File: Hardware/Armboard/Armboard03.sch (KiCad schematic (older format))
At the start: 8 parts

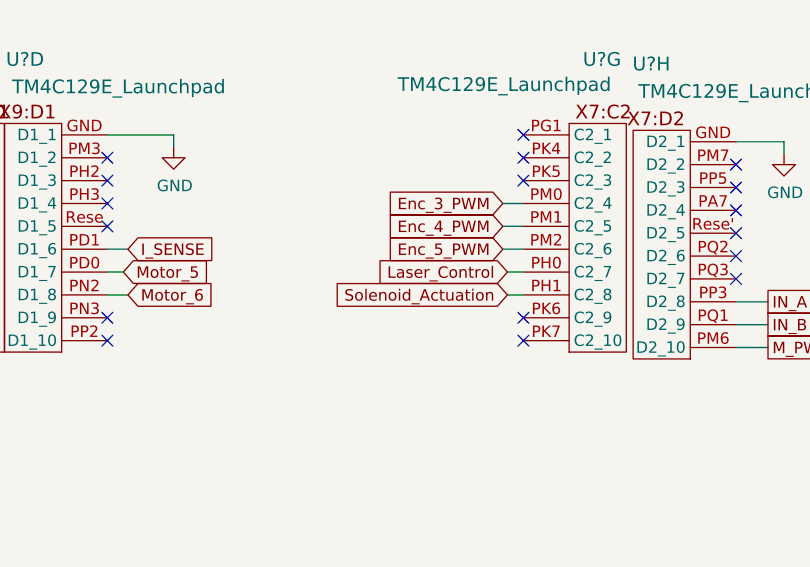
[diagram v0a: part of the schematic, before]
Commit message: Deleted laser and solenoid
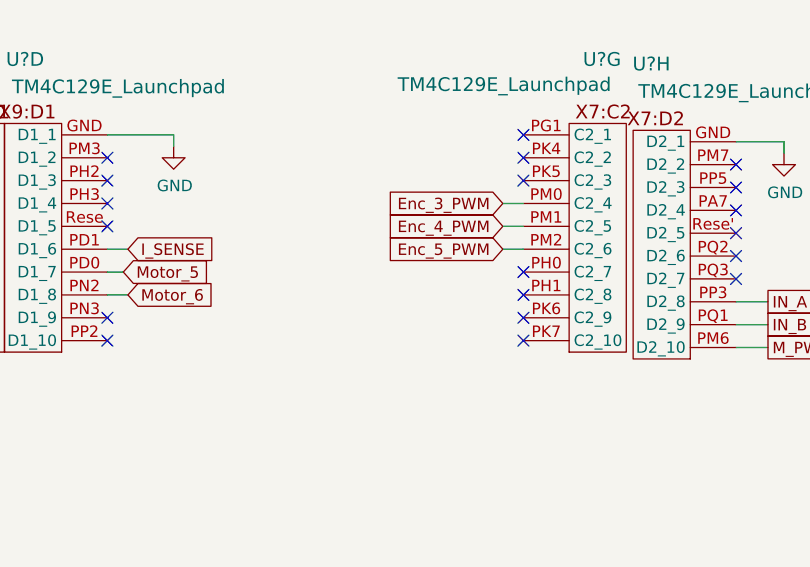
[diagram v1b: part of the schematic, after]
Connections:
- net Laser_Control: no longer names the net of U?.PH0 (C2_7)
- net Solenoid_Actuation: no longer names the net of U?.PH1 (C2_8)
- no-connect marks 43 -> 45
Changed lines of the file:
@@
 $Descr A 11000 8500
 encoding utf-8
-Sheet 3 9
+Sheet 3 7
 Title ""
 Date ""
@@
 Wire Wire Line
 	3610 3350 3540 3350
-Text GLabel 6250 5170 0    50   Input ~ 0
-Laser_Control
-Wire Wire Line
-	6320 5170 6250 5170
-Text GLabel 6250 5270 0    50   Input ~ 0
-Solenoid_Actuation
-Wire Wire Line
-	6320 5270 6250 5270
 Text GLabel 3540 2650 0    50   Input ~ 0
 Rx_1_Tiva
@@
 Wire Wire Line
 	6120 3340 6200 3340
+NoConn ~ 6320 5170
+NoConn ~ 6320 5270
 $EndSCHEMATC

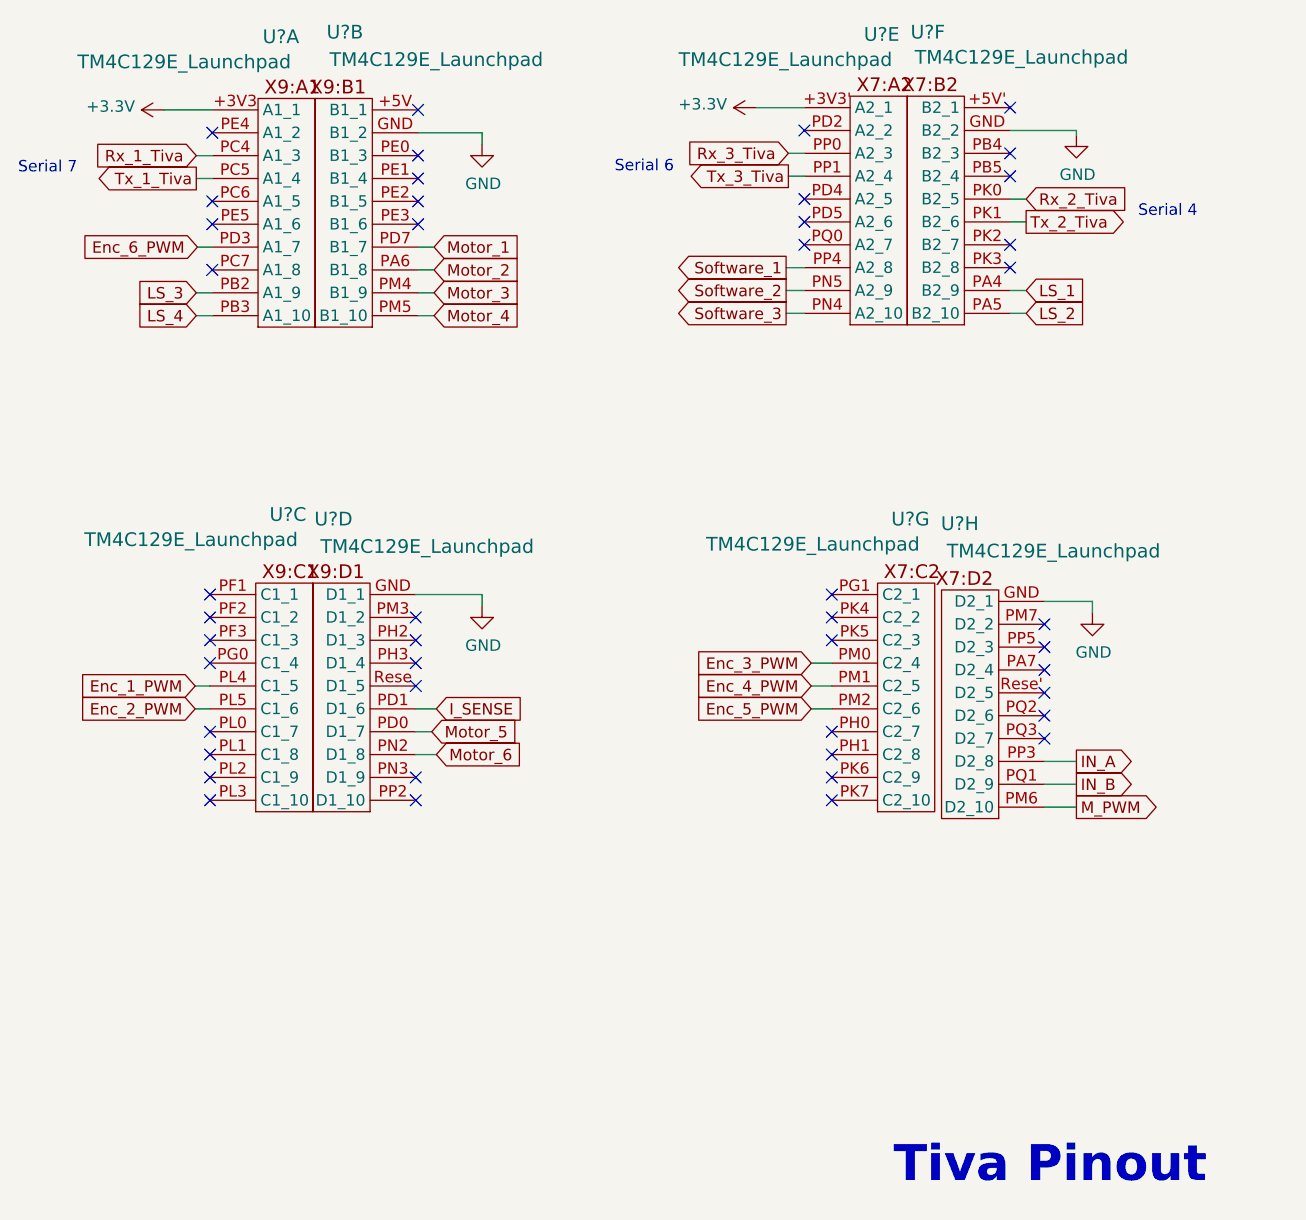
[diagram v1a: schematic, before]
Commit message: Assigned R/L/C footprints
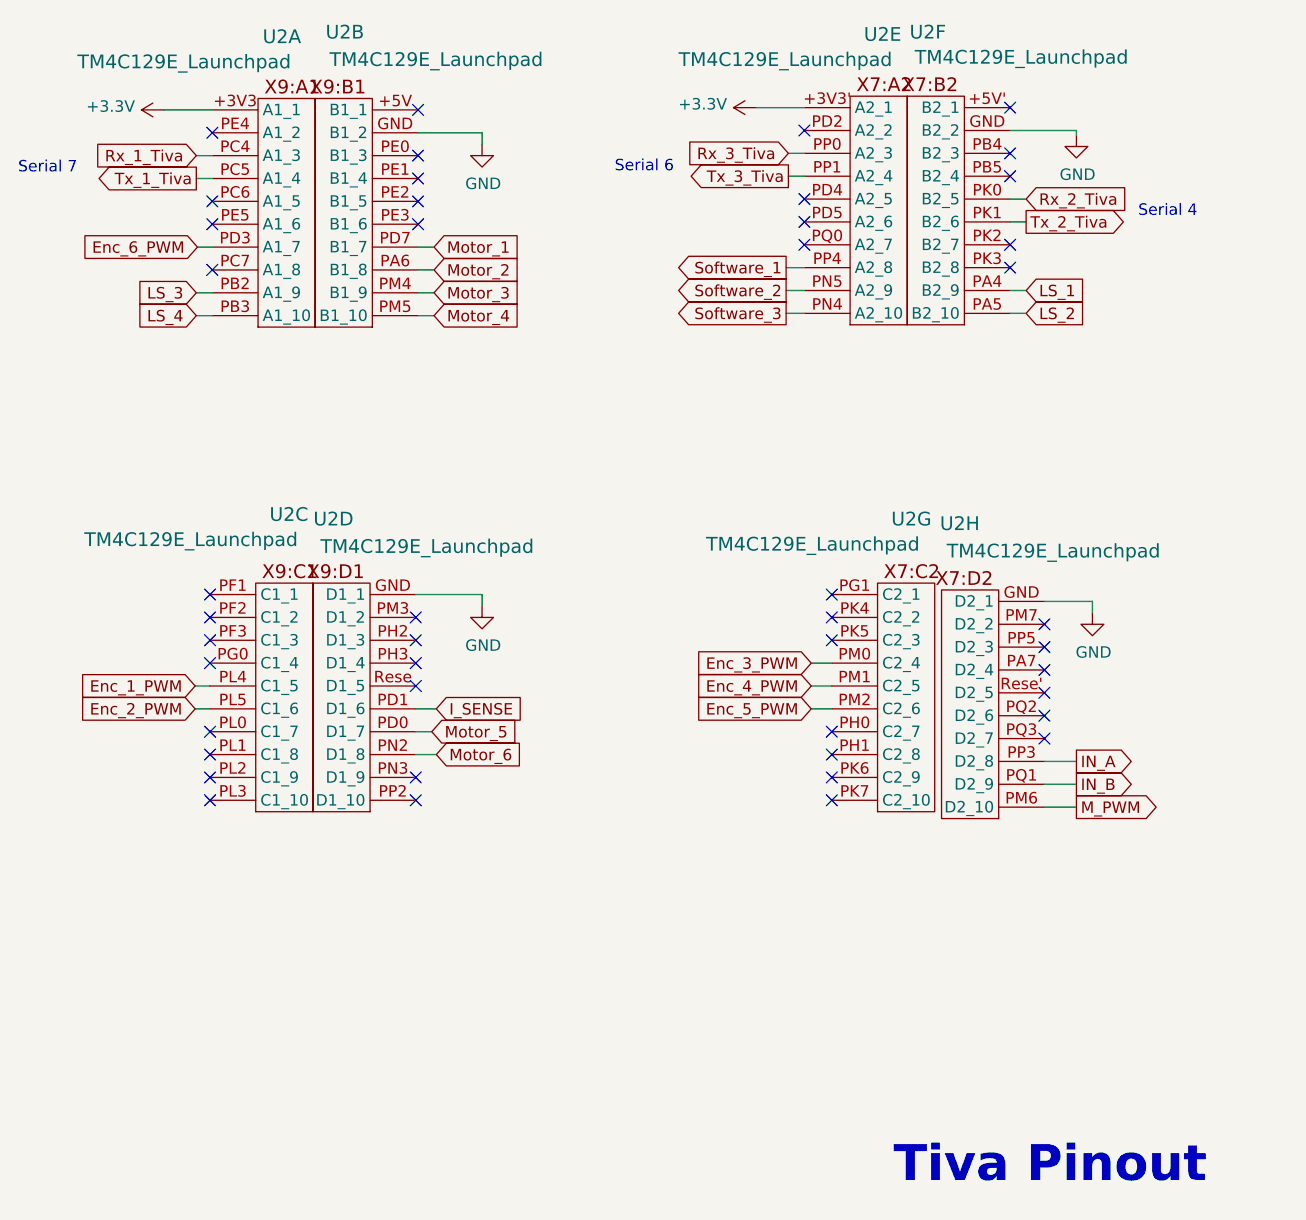
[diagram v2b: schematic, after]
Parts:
- gave numbers to parts that had none: 1
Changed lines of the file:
@@
 $EndDescr
 $Comp
-L Armboard-rescue:TM4C129E_Launchpad-MRDT_Shields-Armboard-rescue U?
+L Armboard-rescue:TM4C129E_Launchpad-MRDT_Shields-Armboard-rescue U2
 U 1 1 5F752485
 P 3810 3400
-F 0 "U?" H 3830 4670 60  0000 L CNN
+F 0 "U2" H 3830 4670 60  0000 L CNN
 F 1 "TM4C129E_Launchpad" H 3020 4560 60  0000 L CNN
 F 2 "" H 3810 3400 60  0001 C CNN
@@
 $EndComp
 $Comp
-L Armboard-rescue:TM4C129E_Launchpad-MRDT_Shields-Armboard-rescue U?
+L Armboard-rescue:TM4C129E_Launchpad-MRDT_Shields-Armboard-rescue U2
 U 2 1 5F752EEB
 P 4310 3400
-F 0 "U?" H 4430 4690 60  0000 C CNN
+F 0 "U2" H 4430 4690 60  0000 C CNN
 F 1 "TM4C129E_Launchpad" H 4030 4570 60  0000 C CNN
 F 2 "" H 4310 3400 60  0001 C CNN
@@
 $EndComp
 $Comp
-L Armboard-rescue:TM4C129E_Launchpad-MRDT_Shields-Armboard-rescue U?
+L Armboard-rescue:TM4C129E_Launchpad-MRDT_Shields-Armboard-rescue U2
 U 3 1 5F753E3C
 P 3800 5520
-F 0 "U?" H 3860 6820 60  0000 L CNN
+F 0 "U2" H 3860 6820 60  0000 L CNN
 F 1 "TM4C129E_Launchpad" H 3050 6710 60  0000 L CNN
 F 2 "" H 3800 5520 60  0001 C CNN
@@
 $EndComp
 $Comp
-L Armboard-rescue:TM4C129E_Launchpad-MRDT_Shields-Armboard-rescue U?
+L Armboard-rescue:TM4C129E_Launchpad-MRDT_Shields-Armboard-rescue U2
 U 5 1 5F755C93
 P 6400 3390
-F 0 "U?" H 6460 4660 60  0000 L CNN
+F 0 "U2" H 6460 4660 60  0000 L CNN
 F 1 "TM4C129E_Launchpad" H 5650 4550 60  0000 L CNN
 F 2 "" H 6400 3390 60  0001 C CNN
@@
 $EndComp
 $Comp
-L Armboard-rescue:TM4C129E_Launchpad-MRDT_Shields-Armboard-rescue U?
+L Armboard-rescue:TM4C129E_Launchpad-MRDT_Shields-Armboard-rescue U2
 U 6 1 5F7570A2
 P 6900 3390
-F 0 "U?" H 7060 4670 60  0000 C CNN
+F 0 "U2" H 7060 4670 60  0000 C CNN
 F 1 "TM4C129E_Launchpad" H 6650 4560 60  0000 C CNN
 F 2 "" H 6900 3390 60  0001 C CNN
@@
 $EndComp
 $Comp
-L Armboard-rescue:TM4C129E_Launchpad-MRDT_Shields-Armboard-rescue U?
+L Armboard-rescue:TM4C129E_Launchpad-MRDT_Shields-Armboard-rescue U2
 U 7 1 5F757FE4
 P 6520 5520
-F 0 "U?" H 6580 6800 60  0000 L CNN
+F 0 "U2" H 6580 6800 60  0000 L CNN
 F 1 "TM4C129E_Launchpad" H 5770 6690 60  0000 L CNN
 F 2 "" H 6520 5520 60  0001 C CNN
@@
 $EndComp
 $Comp
-L Armboard-rescue:TM4C129E_Launchpad-MRDT_Shields-Armboard-rescue U?
+L Armboard-rescue:TM4C129E_Launchpad-MRDT_Shields-Armboard-rescue U2
 U 8 1 5F7598C0
 P 7050 5550
-F 0 "U?" H 7220 6840 60  0000 C CNN
+F 0 "U2" H 7220 6840 60  0000 C CNN
 F 1 "TM4C129E_Launchpad" H 6810 6720 60  0000 C CNN
 F 2 "" H 7050 5550 60  0001 C CNN
@@
 $EndComp
 $Comp
-L power:GND #PWR?
+L power:GND #PWR015
 U 1 1 5F83BEC8
 P 4790 2600
-F 0 "#PWR?" H 4790 2350 50  0001 C CNN
+F 0 "#PWR015" H 4790 2350 50  0001 C CNN
 F 1 "GND" H 4795 2427 50  0000 C CNN
 F 2 "" H 4790 2600 50  0001 C CNN
@@
 	4790 2550 4790 2600
 $Comp
-L power:+3.3V #PWR?
+L power:+3.3V #PWR014
 U 1 1 5F83D247
 P 3400 2450
-F 0 "#PWR?" H 3400 2300 50  0001 C CNN
+F 0 "#PWR014" H 3400 2300 50  0001 C CNN
 F 1 "+3.3V" V 3415 2578 50  0000 L CNN
 F 2 "" H 3400 2450 50  0001 C CNN
@@
 	3400 2450 3610 2450
 $Comp
-L power:+3.3V #PWR?
+L power:+3.3V #PWR017
 U 1 1 5F83FA68
 P 5990 2440
-F 0 "#PWR?" H 5990 2290 50  0001 C CNN
+F 0 "#PWR017" H 5990 2290 50  0001 C CNN
 F 1 "+3.3V" V 6005 2568 50  0000 L CNN
 F 2 "" H 5990 2440 50  0001 C CNN
@@
 	5990 2440 6200 2440
 $Comp
-L power:GND #PWR?
+L power:GND #PWR018
 U 1 1 5F83FD93
 P 7390 2560
-F 0 "#PWR?" H 7390 2310 50  0001 C CNN
+F 0 "#PWR018" H 7390 2310 50  0001 C CNN
 F 1 "GND" H 7395 2387 50  0000 C CNN
 F 2 "" H 7390 2560 50  0001 C CNN
@@
 $EndComp
 $Comp
-L power:GND #PWR?
+L power:GND #PWR016
 U 1 1 5F83FFBB
 P 4790 4620
-F 0 "#PWR?" H 4790 4370 50  0001 C CNN
+F 0 "#PWR016" H 4790 4370 50  0001 C CNN
 F 1 "GND" H 4795 4447 50  0000 C CNN
 F 2 "" H 4790 4620 50  0001 C CNN
@@
 	4790 4570 4790 4620
 $Comp
-L power:GND #PWR?
+L power:GND #PWR019
 U 1 1 5F8401EF
 P 7460 4650
-F 0 "#PWR?" H 7460 4400 50  0001 C CNN
+F 0 "#PWR019" H 7460 4400 50  0001 C CNN
 F 1 "GND" H 7465 4477 50  0000 C CNN
 F 2 "" H 7460 4650 50  0001 C CNN
@@
 	4500 4570 4790 4570
 $Comp
-L Armboard-rescue:TM4C129E_Launchpad-MRDT_Shields-Armboard-rescue U?
+L Armboard-rescue:TM4C129E_Launchpad-MRDT_Shields-Armboard-rescue U2
 U 4 1 5F754D60
 P 4300 5520
-F 0 "U?" H 4460 6800 60  0000 C CNN
+F 0 "U2" H 4460 6800 60  0000 C CNN
 F 1 "TM4C129E_Launchpad" H 4050 6680 60  0000 C CNN
 F 2 "" H 4300 5520 60  0001 C CNN

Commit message: Imported footprints to layout
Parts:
- U2: footprint (none) -> MRDT_Shields:TM4C129E_Launchpad_FULL_SMD_BOTTOM
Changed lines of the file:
@@
 F 0 "U2" H 3830 4670 60  0000 L CNN
 F 1 "TM4C129E_Launchpad" H 3020 4560 60  0000 L CNN
-F 2 "" H 3810 3400 60  0001 C CNN
+F 2 "MRDT_Shields:TM4C129E_Launchpad_FULL_SMD_BOTTOM" H 3810 3400 60  0001 C CNN
 F 3 "" H 3810 3400 60  0001 C CNN
 	1    3810 3400
@@
 F 0 "U2" H 4430 4690 60  0000 C CNN
 F 1 "TM4C129E_Launchpad" H 4030 4570 60  0000 C CNN
-F 2 "" H 4310 3400 60  0001 C CNN
+F 2 "MRDT_Shields:TM4C129E_Launchpad_FULL_SMD_BOTTOM" H 4310 3400 60  0001 C CNN
 F 3 "" H 4310 3400 60  0001 C CNN
 	2    4310 3400
@@
 F 0 "U2" H 3860 6820 60  0000 L CNN
 F 1 "TM4C129E_Launchpad" H 3050 6710 60  0000 L CNN
-F 2 "" H 3800 5520 60  0001 C CNN
+F 2 "MRDT_Shields:TM4C129E_Launchpad_FULL_SMD_BOTTOM" H 3800 5520 60  0001 C CNN
 F 3 "" H 3800 5520 60  0001 C CNN
 	3    3800 5520
@@
 F 0 "U2" H 6460 4660 60  0000 L CNN
 F 1 "TM4C129E_Launchpad" H 5650 4550 60  0000 L CNN
-F 2 "" H 6400 3390 60  0001 C CNN
+F 2 "MRDT_Shields:TM4C129E_Launchpad_FULL_SMD_BOTTOM" H 6400 3390 60  0001 C CNN
 F 3 "" H 6400 3390 60  0001 C CNN
 	5    6400 3390
@@
 F 0 "U2" H 7060 4670 60  0000 C CNN
 F 1 "TM4C129E_Launchpad" H 6650 4560 60  0000 C CNN
-F 2 "" H 6900 3390 60  0001 C CNN
+F 2 "MRDT_Shields:TM4C129E_Launchpad_FULL_SMD_BOTTOM" H 6900 3390 60  0001 C CNN
 F 3 "" H 6900 3390 60  0001 C CNN
 	6    6900 3390
@@
 F 0 "U2" H 6580 6800 60  0000 L CNN
 F 1 "TM4C129E_Launchpad" H 5770 6690 60  0000 L CNN
-F 2 "" H 6520 5520 60  0001 C CNN
+F 2 "MRDT_Shields:TM4C129E_Launchpad_FULL_SMD_BOTTOM" H 6520 5520 60  0001 C CNN
 F 3 "" H 6520 5520 60  0001 C CNN
 	7    6520 5520
@@
 F 0 "U2" H 7220 6840 60  0000 C CNN
 F 1 "TM4C129E_Launchpad" H 6810 6720 60  0000 C CNN
-F 2 "" H 7050 5550 60  0001 C CNN
+F 2 "MRDT_Shields:TM4C129E_Launchpad_FULL_SMD_BOTTOM" H 7050 5550 60  0001 C CNN
 F 3 "" H 7050 5550 60  0001 C CNN
 	8    7050 5550
@@
 F 0 "U2" H 4460 6800 60  0000 C CNN
 F 1 "TM4C129E_Launchpad" H 4050 6680 60  0000 C CNN
-F 2 "" H 4300 5520 60  0001 C CNN
+F 2 "MRDT_Shields:TM4C129E_Launchpad_FULL_SMD_BOTTOM" H 4300 5520 60  0001 C CNN
 F 3 "" H 4300 5520 60  0001 C CNN
 	4    4300 5520

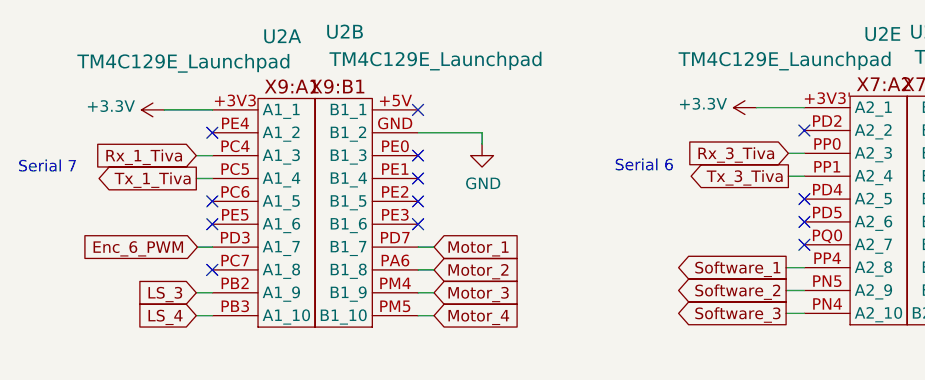
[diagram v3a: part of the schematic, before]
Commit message: Double-checked schematic, pointed power pins up, made sure 12V and 3.3V were full networks
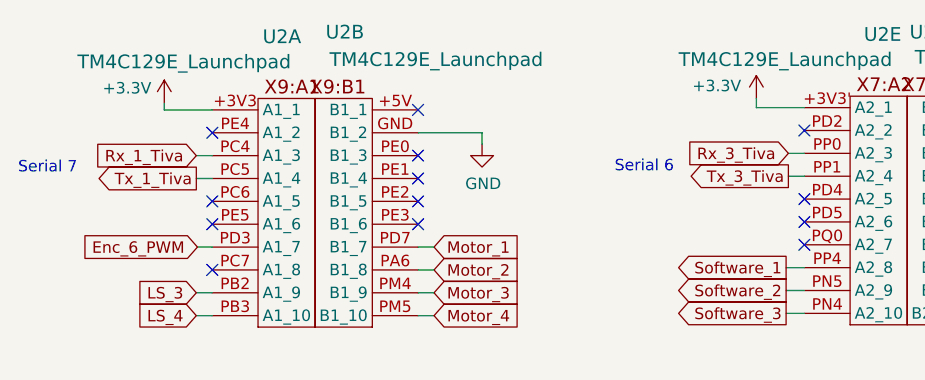
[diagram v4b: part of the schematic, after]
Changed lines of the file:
@@
 L power:+3.3V #PWR014
 U 1 1 5F83D247
-P 3400 2450
-F 0 "#PWR014" H 3400 2300 50  0001 C CNN
-F 1 "+3.3V" V 3415 2578 50  0000 L CNN
-F 2 "" H 3400 2450 50  0001 C CNN
-F 3 "" H 3400 2450 50  0001 C CNN
-	1    3400 2450
-	0    -1   -1   0
+P 3400 2420
+F 0 "#PWR014" H 3400 2270 50  0001 C CNN
+F 1 "+3.3V" H 3130 2485 50  0000 L CNN
+F 2 "" H 3400 2420 50  0001 C CNN
+F 3 "" H 3400 2420 50  0001 C CNN
+	1    3400 2420
+	1    0    0    -1
 $EndComp
 Wire Wire Line
@@
 L power:+3.3V #PWR017
 U 1 1 5F83FA68
-P 5990 2440
-F 0 "#PWR017" H 5990 2290 50  0001 C CNN
-F 1 "+3.3V" V 6005 2568 50  0000 L CNN
-F 2 "" H 5990 2440 50  0001 C CNN
-F 3 "" H 5990 2440 50  0001 C CNN
-	1    5990 2440
-	0    -1   -1   0
+P 5990 2400
+F 0 "#PWR017" H 5990 2250 50  0001 C CNN
+F 1 "+3.3V" H 5710 2455 50  0000 L CNN
+F 2 "" H 5990 2400 50  0001 C CNN
+F 3 "" H 5990 2400 50  0001 C CNN
+	1    5990 2400
+	1    0    0    -1
 $EndComp
 Wire Wire Line
@@
 NoConn ~ 6320 5170
 NoConn ~ 6320 5270
+Wire Wire Line
+	3400 2450 3400 2420
+Wire Wire Line
+	5990 2440 5990 2400
 $EndSCHEMATC

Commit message: Fixed some library issues and moved Gerbs to Manufacturing folder
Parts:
- U2: symbol Armboard-rescue:TM4C129E_Launchpad-MRDT_Shields-Armboard-rescue -> MRDT_Shields:TM4C129E_Launchpad
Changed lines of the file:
@@
 EESchema Schematic File Version 4
+LIBS:Armboard-cache
 EELAYER 30 0
 EELAYER END
@@
 $EndDescr
 $Comp
-L Armboard-rescue:TM4C129E_Launchpad-MRDT_Shields-Armboard-rescue U2
+L MRDT_Shields:TM4C129E_Launchpad U2
 U 1 1 5F752485
 P 3810 3400
@@
 $EndComp
 $Comp
-L Armboard-rescue:TM4C129E_Launchpad-MRDT_Shields-Armboard-rescue U2
+L MRDT_Shields:TM4C129E_Launchpad U2
 U 2 1 5F752EEB
 P 4310 3400
@@
 $EndComp
 $Comp
-L Armboard-rescue:TM4C129E_Launchpad-MRDT_Shields-Armboard-rescue U2
+L MRDT_Shields:TM4C129E_Launchpad U2
 U 3 1 5F753E3C
 P 3800 5520
@@
 $EndComp
 $Comp
-L Armboard-rescue:TM4C129E_Launchpad-MRDT_Shields-Armboard-rescue U2
+L MRDT_Shields:TM4C129E_Launchpad U2
 U 5 1 5F755C93
 P 6400 3390
@@
 $EndComp
 $Comp
-L Armboard-rescue:TM4C129E_Launchpad-MRDT_Shields-Armboard-rescue U2
+L MRDT_Shields:TM4C129E_Launchpad U2
 U 6 1 5F7570A2
 P 6900 3390
@@
 $EndComp
 $Comp
-L Armboard-rescue:TM4C129E_Launchpad-MRDT_Shields-Armboard-rescue U2
+L MRDT_Shields:TM4C129E_Launchpad U2
 U 7 1 5F757FE4
 P 6520 5520
@@
 $EndComp
 $Comp
-L Armboard-rescue:TM4C129E_Launchpad-MRDT_Shields-Armboard-rescue U2
+L MRDT_Shields:TM4C129E_Launchpad U2
 U 8 1 5F7598C0
 P 7050 5550
@@
 	4500 4570 4790 4570
 $Comp
-L Armboard-rescue:TM4C129E_Launchpad-MRDT_Shields-Armboard-rescue U2
+L MRDT_Shields:TM4C129E_Launchpad U2
 U 4 1 5F754D60
 P 4300 5520
